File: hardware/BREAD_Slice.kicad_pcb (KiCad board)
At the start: 2 copper layers, 70 x 100 mm, 23 parts, among them J1 Conn_01x10_Female, J2 Screw_Terminal_01x02, J3 Screw_Terminal_01x02, J4 Screw_Terminal_01x02, J5 Screw_Terminal_01x02, U2 ACS723xMATR-10AB, U3 ACS723xMATR-10AB, U4 ACS723xMATR-10AB, U5 ACS723xMATR-10AB

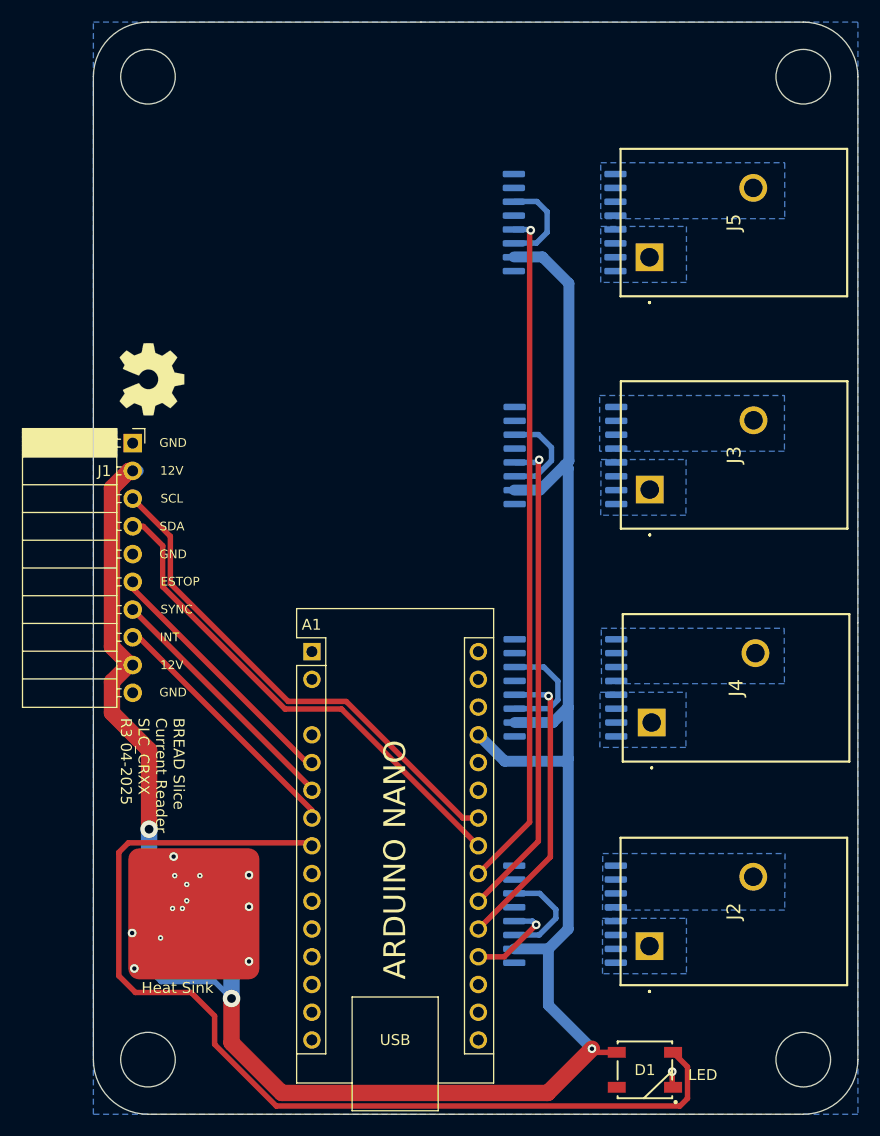
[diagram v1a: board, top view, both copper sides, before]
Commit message: initial commit after split of ac and dc
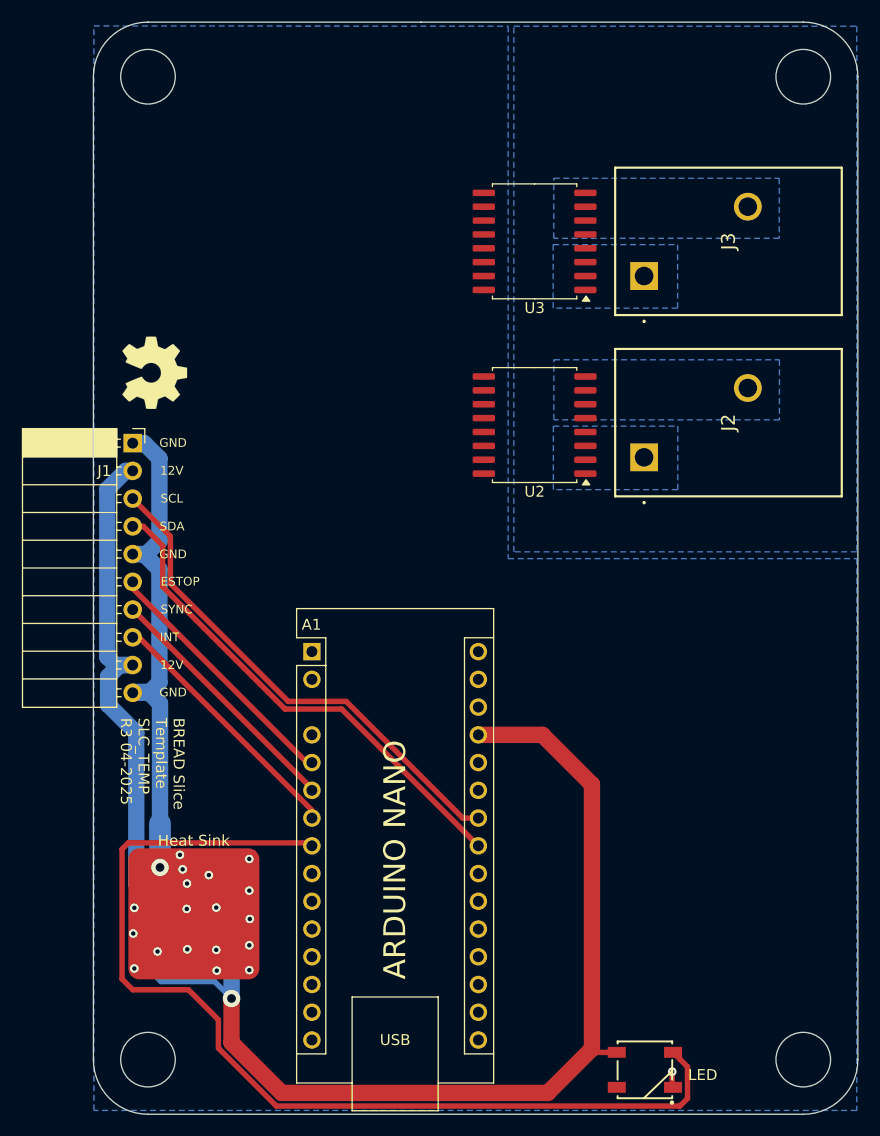
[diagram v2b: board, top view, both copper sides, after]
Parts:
- removed J4, J5: Screw_Terminal_01x02, CRx:Pheonix Conn Term TDPT 4 2-SP-6,35-ZB
- removed U4, U5: ACS723xMATR-10AB, Package_SO:SOIC-16W_7.5x10.3mm_P1.27mm
- added NT1: NetTie_2, NetTie:NetTie-2_SMD_Pad2.0mm, B.Cu at (128.7, 115.2)
- HS1: footprint KML-Custom:Thermal Pad -> kml-custom:Thermal Pad
- U1: value ~ -> AP63205
- U2, U3: moved to F.Cu
- moved U2 44.9 mm to (163.0, 76.7)
- moved J2 44.8 mm to (173.0, 79.7)
- moved U3 19.8 mm to (163.0, 59.9)
- moved J3 19.6 mm to (173.0, 63.0)
- moved Logo1 0.65 mm to (128.2, 71.9)
- moved C4 0.05 mm to (133.8, 116.4)
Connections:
- net /E_STOP renamed /ESTOP
- A1 pad 10: /D7 -> unconnected-(A1-D7-Pad10)
- A1 pad 11: /D8 -> unconnected-(A1-D8-Pad11)
- A1 pad 12: /D9 -> unconnected-(A1-D9-Pad12)
- A1 pad 13: /D10 -> unconnected-(A1-D10-Pad13)
- A1 pad 14: /D11 -> unconnected-(A1-D11-Pad14)
- A1 pad 15: /D12 -> unconnected-(A1-D12-Pad15)
- A1 pad 16: /D13 -> unconnected-(A1-D13-Pad16)
- A1 pad 18: /AREF -> unconnected-(A1-AREF-Pad18)
- A1 pad 21: /CURR3 -> unconnected-(A1-A2-Pad21)
- A1 pad 22: /CURR4 -> unconnected-(A1-A3-Pad22)
- A1 pad 25: /A6 -> unconnected-(A1-A6-Pad25)
- A1 pad 26: /A7 -> unconnected-(A1-A7-Pad26)
- A1 pad 28: /RESET -> unconnected-(A1-~{RESET}-Pad28)
- A1 pad 9: /D6 -> unconnected-(A1-D6-Pad9)
- J1 pad 1: GND -> GNDPWR
- J1 pad 10: GND -> GNDPWR
- J1 pad 5: GND -> GNDPWR
- J2 pad 1: Net-(J2-Pin_1) -> /Input1+
- J2 pad 2: Net-(J2-Pin_2) -> /Input1-
- J3 pad 1: Net-(J3-Pin_1) -> /Input2+
- J3 pad 2: Net-(J3-Pin_2) -> /Input2-
- U2 pad 1: Net-(J2-Pin_2) -> /Input1+
- U2 pad 2: Net-(J2-Pin_2) -> /Input1+
- U2 pad 3: Net-(J2-Pin_2) -> /Input1+
- U2 pad 4: Net-(J2-Pin_2) -> /Input1+
- U2 pad 5: Net-(J2-Pin_1) -> /Input1-
- U2 pad 6: Net-(J2-Pin_1) -> /Input1-
- U2 pad 7: Net-(J2-Pin_1) -> /Input1-
- U2 pad 8: Net-(J2-Pin_1) -> /Input1-
- U3 pad 1: Net-(J3-Pin_2) -> /Input2+
- U3 pad 12: /CURR3 -> /CURR2
- U3 pad 2: Net-(J3-Pin_2) -> /Input2+
- U3 pad 3: Net-(J3-Pin_2) -> /Input2+
- U3 pad 4: Net-(J3-Pin_2) -> /Input2+
- U3 pad 5: Net-(J3-Pin_1) -> /Input2-
- U3 pad 6: Net-(J3-Pin_1) -> /Input2-
- U3 pad 7: Net-(J3-Pin_1) -> /Input2-
- U3 pad 8: Net-(J3-Pin_1) -> /Input2-
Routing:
- net +5V: track 170.1 -> 104.2 mm, vias 2 -> 1
- net /CURR4: track 62.5 -> 0.00 mm, vias 1 -> 0
- net /CURR3: track 45.1 -> 0.00 mm, vias 1 -> 0
- net GNDPWR: track 0.00 -> 43.7 mm
- net GND: track 55.7 -> 16.8 mm, vias 14 -> 20
- net /CURR2: track 27.3 -> 0.00 mm, vias 1 -> 0
- net /CURR1: track 8.65 -> 0.00 mm, vias 1 -> 0
- net +12V: track 46.9 -> 48.2 mm, vias 1 -> 0
- added copper zone on B.Cu, net (none)
- added copper zone on B.Cu, net /Input1+
- added copper zone on B.Cu, net /Input1-
- added copper zone on B.Cu, net /Input2+
- added copper zone on B.Cu, net /Input2-
- removed copper zone on B.Cu, net Net-(J2-Pin_1)
- removed copper zone on B.Cu, net Net-(J2-Pin_2)
- removed copper zone on B.Cu, net Net-(J3-Pin_1)
- removed copper zone on B.Cu, net Net-(J3-Pin_2)
- removed copper zone on B.Cu, net Net-(J4-Pin_1)
- removed copper zone on B.Cu, net Net-(J4-Pin_2)
- removed copper zone on B.Cu, net Net-(J5-Pin_1)
- removed copper zone on B.Cu, net Net-(J5-Pin_2)
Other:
- outline, holes or cut-outs redrawn
- board text added: "BREAD Slice Template SLC_TEMP R3 04-2025"
- board text removed: "BREAD Slice Current Reader SLC_CRXX R3 04-2025"

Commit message: minor tweaks
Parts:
- removed U2, U3: ACS723xMATR-10AB, Package_SO:SOIC-16W_7.5x10.3mm_P1.27mm

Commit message: completed board
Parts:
- removed J3: Screw_Terminal_01x02, CRx:Pheonix Conn Term TDPT 4 2-SP-6,35-ZB
- added C10: 100n, Capacitor_SMD:C_0603_1608Metric_Pad1.08x0.95mm_HandSolder, B.Cu at (154.9, 67.9)
- added C11: 0.1u, Capacitor_SMD:C_0603_1608Metric_Pad1.08x0.95mm_HandSolder, B.Cu at (152.1, 58.0)
- added C12: 100p, Capacitor_SMD:C_0603_1608Metric_Pad1.08x0.95mm_HandSolder, B.Cu at (154.0, 70.4)
- added C13: 10n, Capacitor_SMD:C_0603_1608Metric_Pad1.08x0.95mm_HandSolder, B.Cu at (148.0, 55.3)
- added C14: 10n, Capacitor_SMD:C_0603_1608Metric_Pad1.08x0.95mm_HandSolder, B.Cu at (136.7, 57.1)
- added C15: 0.1u, Capacitor_SMD:C_0603_1608Metric_Pad1.08x0.95mm_HandSolder, B.Cu at (135.0, 57.1)
- added C16: 330p, Capacitor_SMD:C_0805_2012Metric_Pad1.18x1.45mm_HandSolder, B.Cu at (135.3, 65.4)
- added C17: 10u, Capacitor_SMD:C_0603_1608Metric_Pad1.08x0.95mm_HandSolder, B.Cu at (133.3, 57.1)
- added C18: 1u, Capacitor_SMD:C_0805_2012Metric_Pad1.18x1.45mm_HandSolder, B.Cu at (139.9, 66.5)
- added C19: 330p, Capacitor_SMD:C_0805_2012Metric_Pad1.18x1.45mm_HandSolder, B.Cu at (133.6, 74.5)
- added C20: 100n, Capacitor_SMD:C_0805_2012Metric_Pad1.18x1.45mm_HandSolder, B.Cu at (139.9, 64.4)
- added C21: 0.1u, Capacitor_SMD:C_0805_2012Metric_Pad1.18x1.45mm_HandSolder, B.Cu at (130.8, 67.2)
- added C5: 1n, Capacitor_SMD:C_0805_2012Metric_Pad1.18x1.45mm_HandSolder, B.Cu at (155.5, 55.2)
- added C6: 0.1u, Capacitor_SMD:C_0805_2012Metric_Pad1.18x1.45mm_HandSolder, B.Cu at (157.6, 55.2)
- added C7: 1n, Capacitor_SMD:C_0805_2012Metric_Pad1.18x1.45mm_HandSolder, B.Cu at (156.5, 60.5)
- added C8: 1u, Capacitor_SMD:C_0603_1608Metric_Pad1.08x0.95mm_HandSolder, B.Cu at (154.9, 66.2)
- added C9: 10u, Capacitor_SMD:C_0603_1608Metric_Pad1.08x0.95mm_HandSolder, B.Cu at (151.2, 55.3)
- added NT2: NetTie_2, NetTie:NetTie-2_SMD_Pad0.5mm, B.Cu at (161.8, 67.0)
- added R1: 1k, Resistor_SMD:R_0805_2012Metric_Pad1.20x1.40mm_HandSolder, B.Cu at (156.5, 58.2)
- added R2: 16.9k, Resistor_SMD:R_0603_1608Metric_Pad0.98x0.95mm_HandSolder, B.Cu at (149.6, 57.1)
- added R3: 10k, Resistor_SMD:R_0603_1608Metric_Pad0.98x0.95mm_HandSolder, B.Cu at (148.0, 58.9)
- added R4: 3.3k, Resistor_SMD:R_0805_2012Metric_Pad1.20x1.40mm_HandSolder, B.Cu at (137.5, 71.2)
- added R5: 3.3k, Resistor_SMD:R_0805_2012Metric_Pad1.20x1.40mm_HandSolder, B.Cu at (137.5, 69.2)
- added R6: 3.3k, Resistor_SMD:R_0805_2012Metric_Pad1.20x1.40mm_HandSolder, B.Cu at (133.0, 65.4)
- added R7: 10k, Resistor_SMD:R_0805_2012Metric_Pad1.20x1.40mm_HandSolder, B.Cu at (128.4, 69.4)
- added R8: 10k, Resistor_SMD:R_0805_2012Metric_Pad1.20x1.40mm_HandSolder, B.Cu at (130.5, 71.3)
- added R9: 3.3k, Resistor_SMD:R_0805_2012Metric_Pad1.20x1.40mm_HandSolder, B.Cu at (133.6, 76.6)
- added RSNS1: 20.05k 1%, Resistor_SMD:R_1206_3216Metric_Pad1.30x1.75mm_HandSolder, B.Cu at (162.2, 69.6)
- added RX1: 665k 1%, Resistor_SMD:R_1206_3216Metric_Pad1.30x1.75mm_HandSolder, B.Cu at (177.5, 77.8)
- added RX2: 665k 1%, Resistor_SMD:R_1206_3216Metric_Pad1.30x1.75mm_HandSolder, B.Cu at (172.3, 77.8)
- added RX3: 665k 1%, Resistor_SMD:R_1206_3216Metric_Pad1.30x1.75mm_HandSolder, B.Cu at (167.2, 77.8)
- added RX4: 665k 1%, Resistor_SMD:R_1206_3216Metric_Pad1.30x1.75mm_HandSolder, B.Cu at (162.1, 77.8)
- added RX5: 665k 1%, Resistor_SMD:R_1206_3216Metric_Pad1.30x1.75mm_HandSolder, B.Cu at (158.3, 76.3)
- added RX6: 665k 1%, Resistor_SMD:R_1206_3216Metric_Pad1.30x1.75mm_HandSolder, B.Cu at (158.3, 71.1)
- added U2: ACS724xLCTR-50AB, Package_SO:SOIC-8_3.9x4.9mm_P1.27mm, B.Cu at (163.0, 58.9)
- added U3: AMC1311BDWVR, kml-custom:DWV0008A, B.Cu at (146.4, 70.2)
- added U4: ADUM5010ARSZ-RL7, kml-custom:RS_20_ADI, B.Cu at (142.4, 58.5)
- added U5: TLV9001IDCK, Package_TO_SOT_SMD:SOT-353_SC-70-5, B.Cu at (133.6, 68.9)
- added U6: TLV9001IDCK, Package_TO_SOT_SMD:SOT-353_SC-70-5, B.Cu at (133.7, 71.9)
- J2: value Screw_Terminal_01x02 -> 2606-1104/010-000; footprint CRx:Pheonix Conn Term TDPT 4 2-SP-6,35-ZB -> kml-custom:CONN4_2606-1104&slash_010-000_WAG
- moved J2 9.11 mm to (181.9, 77.8)
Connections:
- A1 pad 20: /CURR2 -> unconnected-(A1-A1-Pad20)
- A1 pad 21: unconnected-(A1-A2-Pad21) -> /VOLT1
- A1 pad 9: unconnected-(A1-D6-Pad9) -> /ISO_DIS
- J2 pad 1: /Input1+ -> /Isolated DC Voltage Sensor1/DC_BUS+
- J2 pad 2: /Input1- -> /Isolated DC Voltage Sensor1/DC_BUS-
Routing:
- net +5V: track 104.2 -> 231.1 mm, vias 1 -> 6
- net /ISO_DIS: track 0.00 -> 89.5 mm
- net /VOLT1: track 0.00 -> 70.2 mm
- net /Isolated DC Voltage Sensor1/GNDISO: track 0.00 -> 47.9 mm, vias 0 -> 2
- net GND: track 16.8 -> 46.9 mm, vias 20 -> 24
- net /Isolated DC Voltage Sensor1/VDD_ISO: track 0.00 -> 20.4 mm
- net Net-(U6-+): track 0.00 -> 10.5 mm
- net /Isolated DC Voltage Sensor1/DC_BUS-: track 0.00 -> 9.57 mm
- net /Isolated DC Voltage Sensor1/VIN: track 0.00 -> 8.81 mm, vias 0 -> 2
- net Net-(U5-+): track 0.00 -> 8.53 mm, vias 0 -> 2
- net /Isolated DC Voltage Sensor1/VREF: track 0.00 -> 6.63 mm
- net Net-(U6--): track 0.00 -> 6.55 mm
- net /Isolated DC Voltage Sensor1/VSEL: track 0.00 -> 4.13 mm
- net Net-(U2-FILTER): track 0.00 -> 3.38 mm
- net /Isolated DC Voltage Sensor1/DC_BUS+: track 0.00 -> 2.94 mm
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- added copper zone on B.Cu, net /Invasive Isolated AC-DC Current Sensor1/IC_CS_Input+
- added copper zone on B.Cu, net /Invasive Isolated AC-DC Current Sensor1/IC_CS_Input-
- removed copper zone on B.Cu, net (none)
- removed copper zone on B.Cu, net /Input1+
- removed copper zone on B.Cu, net /Input1-
- removed copper zone on B.Cu, net /Input2+
- removed copper zone on B.Cu, net /Input2-
